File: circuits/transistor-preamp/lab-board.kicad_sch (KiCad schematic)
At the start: 32 parts, among them J1 Conn_01x02, J2 Conn_01x02, J3 Conn_01x02, Q1 2N3904

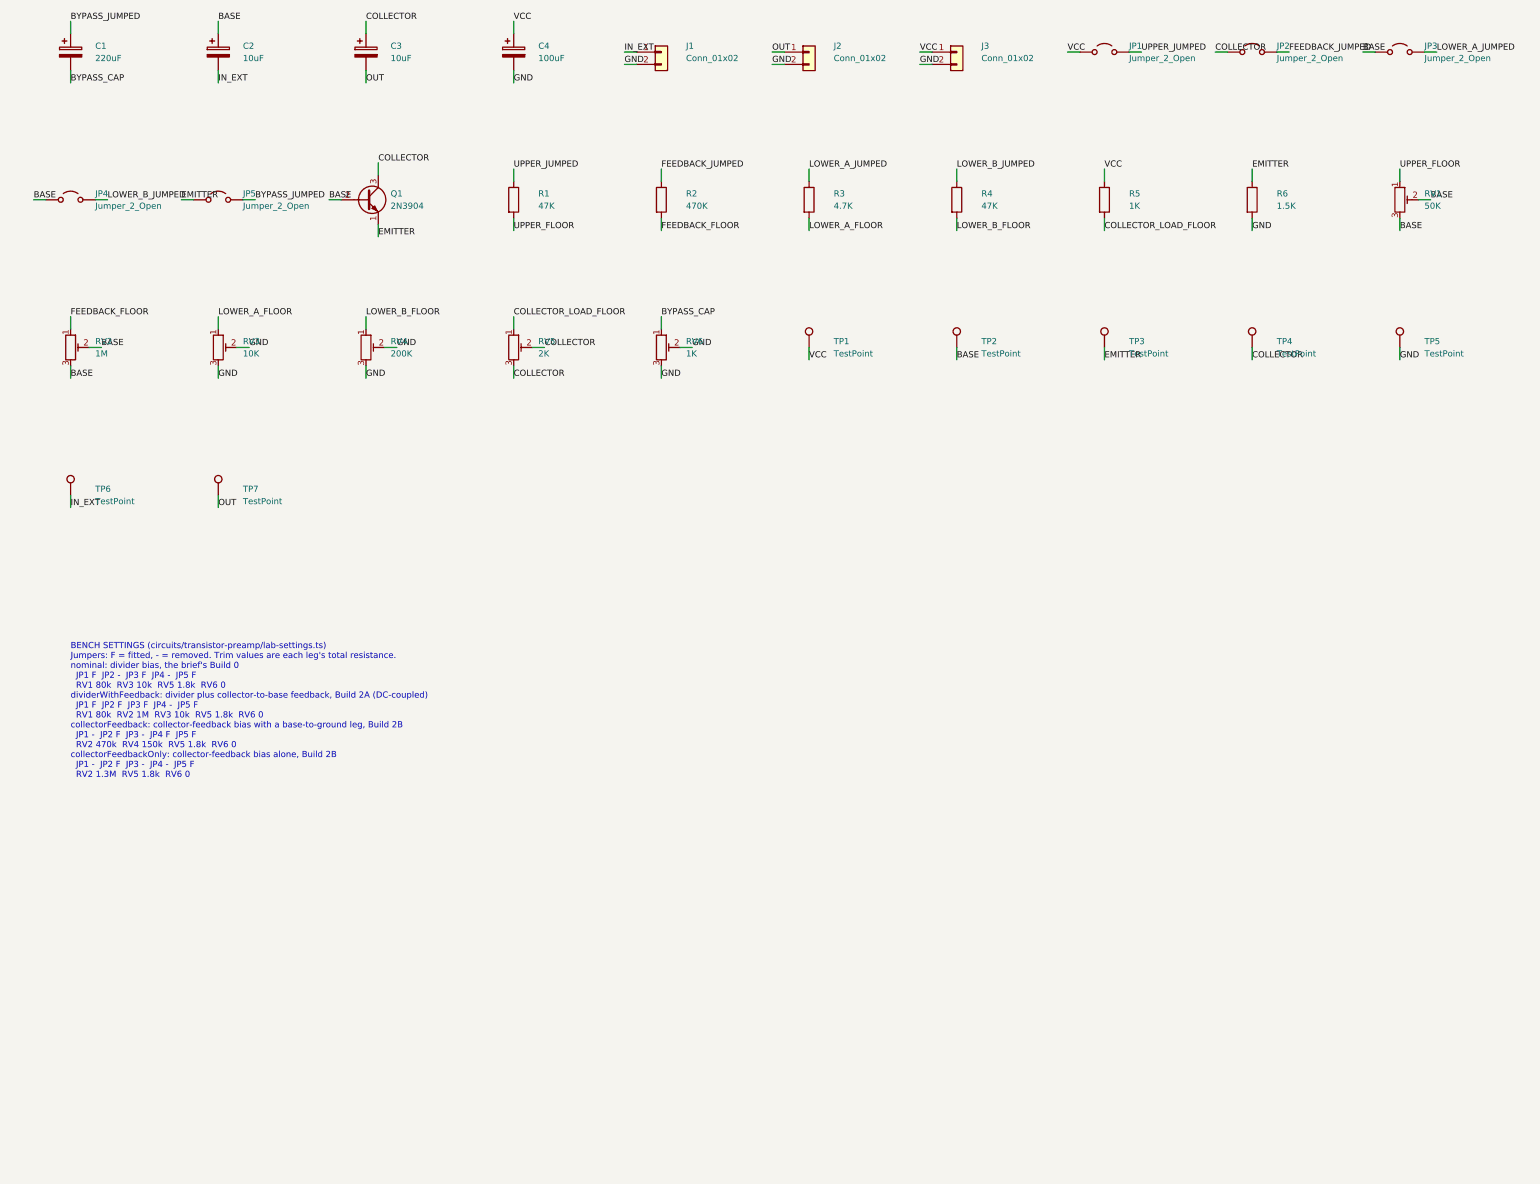
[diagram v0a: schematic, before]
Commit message: Regenerate the lab board's schematic stub with the corrected placement order
The committed stub was generated before the writer placed parts by
declaration order instead of designator sort. Regenerate it with
`bun run schematic-stub`, and let `make netlist-agrees` refresh the netlist
fixture from it - only per-instance UUIDs and the volatile date line moved;
every designator, value, footprint and net membership is unchanged, and
tests/circuits/transistor-preamp-lab.test.ts still passes against it.
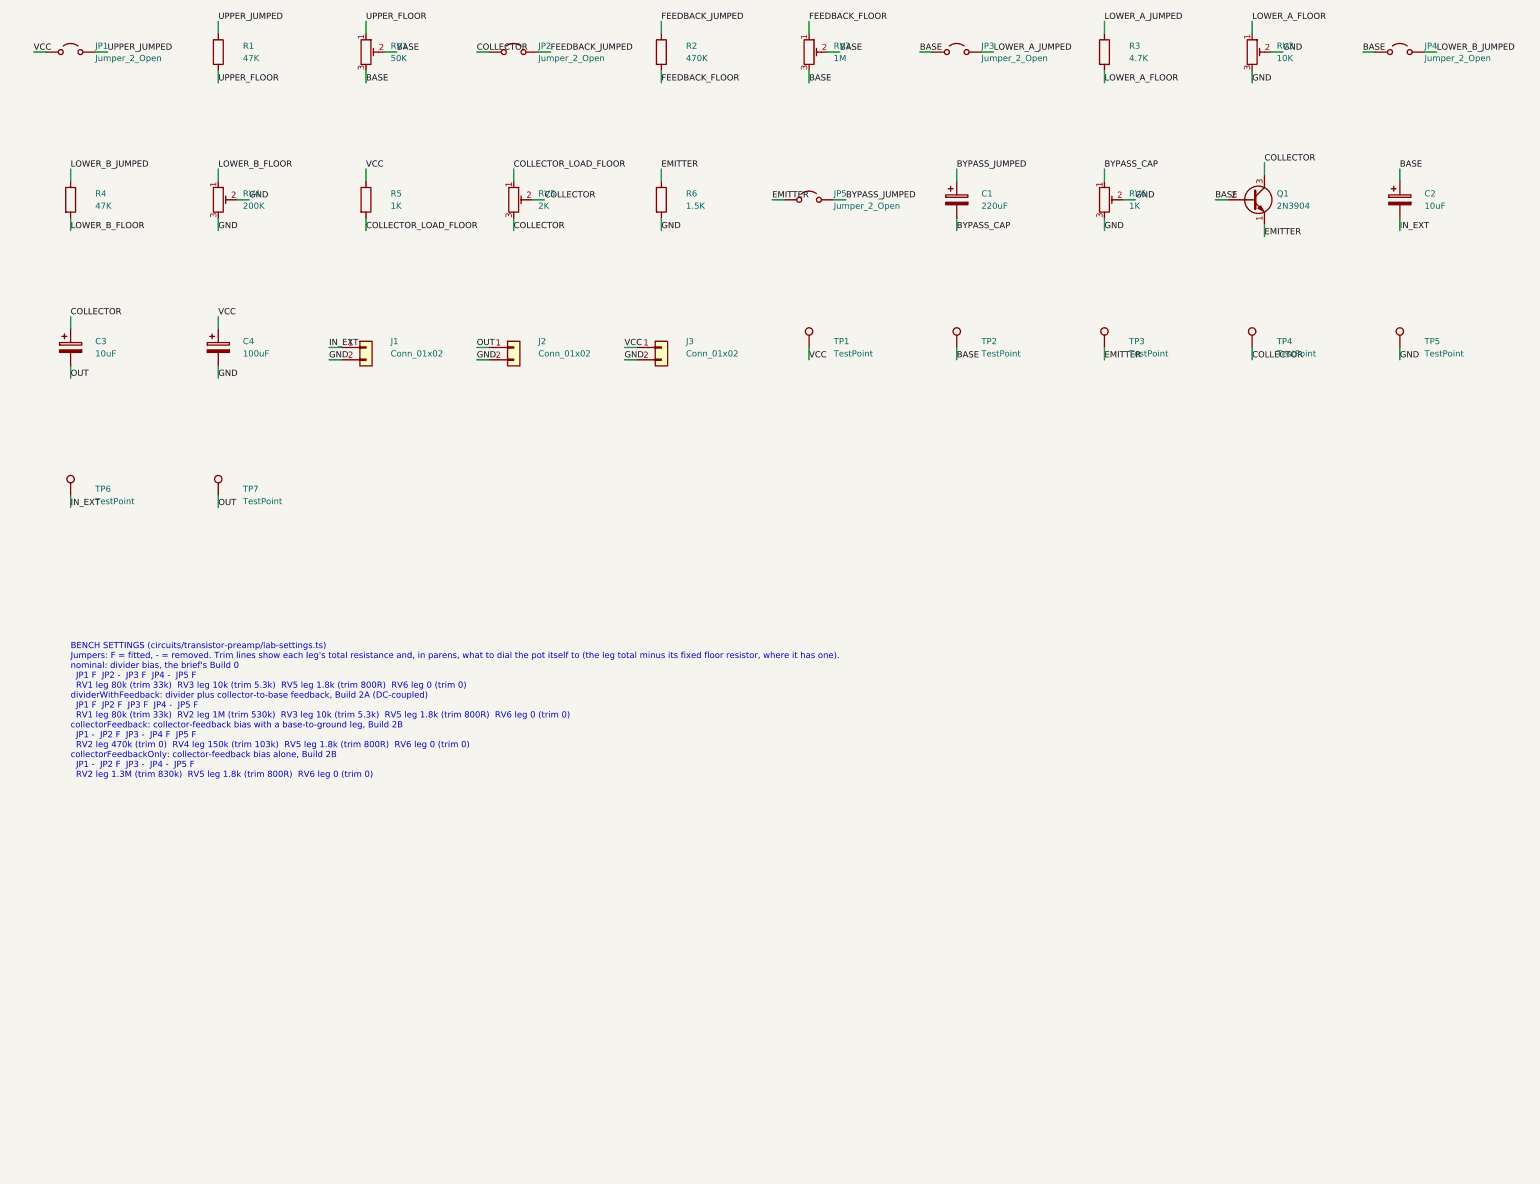
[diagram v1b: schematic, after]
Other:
- note added: "BENCH SETTINGS (circuits/transistor-preamp/lab-settings.ts) Jumpers: F = fitted, - = removed. Trim lines show each leg's total resistance and, in parens, what to dial the pot itself to (the leg total minus its fixed floor resistor, where it has one). nominal: divider bias, the brief's Build 0 JP1 F JP2 - JP3 F JP4 - JP5 F RV1 leg 80k (trim 33k) RV3 leg 10k (trim 5.3k) RV5 leg 1.8k (trim 800R) RV6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"
- note removed: "BENCH SETTINGS (circuits/transistor-preamp/lab-settings.ts) Jumpers: F = fitted, - = removed. Trim values are each leg's total resistance. nominal: divider bias, the brief's Build 0 JP1 F JP2 - JP3 F JP4 - JP5 F RV1 80k RV3 10k RV5 1.8k RV6 0 dividerWithFeedback: divider plus collector-to-base feedback, Build 2A (DC-coupled) JP1 F JP2 F JP3 F JP4 - JP5 F RV1 80k RV2 1M RV3 10k RV5 1.8k RV6 0 coll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"

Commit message: layout
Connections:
- net VCC is gone; now on net COLLECTOR: C4.1, J3.1 (Pin_1), JP1.1 (A), R5.1, TP1.1
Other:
- moved on the sheet: C1, C2, C3, C4, J1, J2, J3, JP1, JP2, JP3, JP4, JP5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

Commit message: repair
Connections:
- net COLLECTOR: no longer C4.1, J3.1 (Pin_1), JP1.1 (A), R5.1, TP1.1
- new net VCC: C4.1, J3.1 (Pin_1), JP1.1 (A), R5.1, TP1.1
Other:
- moved on the sheet: C4, J3, R5, RV5, TP1, TP4

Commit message: Use the Runtron RM-065 trimmers on hand instead of the Bourns 3006P
The 3006P is a 19 mm long 15-turn part, and VeroRoute draws it at half its real width. The RM-065 maps to VeroRoute's TRIM_FLAT, whose pin pattern matches the RM065 datasheet and KiCad's footprint.
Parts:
- RV1, RV2, RV3, RV4, RV5, RV6: footprint Potentiometer_THT:Potentiometer_Bourns_3006P_Horizontal -> Potentiometer_THT:Potentiometer_Runtron_RM-065_Vertical
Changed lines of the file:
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@@
 			)
 		)
-		(property "Footprint" "Potentiometer_THT:Potentiometer_Bourns_3006P_Horizontal"
+		(property "Footprint" "Potentiometer_THT:Potentiometer_Runtron_RM-065_Vertical"
 			(at 124.46 191.77 0)
 			(hide yes)
@@
 			)
 		)
-		(property "Footprint" "Potentiometer_THT:Potentiometer_Bourns_3006P_Horizontal"
+		(property "Footprint" "Potentiometer_THT:Potentiometer_Runtron_RM-065_Vertical"
 			(at 88.9 110.49 0)
 			(hide yes)
@@
 			)
 		)
-		(property "Footprint" "Potentiometer_THT:Potentiometer_Bourns_3006P_Horizontal"
+		(property "Footprint" "Potentiometer_THT:Potentiometer_Runtron_RM-065_Vertical"
 			(at 151.13 67.31 0)
 			(hide yes)
@@
 			)
 		)
-		(property "Footprint" "Potentiometer_THT:Potentiometer_Bourns_3006P_Horizontal"
+		(property "Footprint" "Potentiometer_THT:Potentiometer_Runtron_RM-065_Vertical"
 			(at 120.65 110.49 0)
 			(hide yes)
@@
 			)
 		)
-		(property "Footprint" "Potentiometer_THT:Potentiometer_Bourns_3006P_Horizontal"
+		(property "Footprint" "Potentiometer_THT:Potentiometer_Runtron_RM-065_Vertical"
 			(at 168.91 191.77 0)
 			(hide yes)
@@
 			)
 		)
-		(property "Footprint" "Potentiometer_THT:Potentiometer_Bourns_3006P_Horizontal"
+		(property "Footprint" "Potentiometer_THT:Potentiometer_Runtron_RM-065_Vertical"
 			(at 82.55 191.77 0)
 			(hide yes)
